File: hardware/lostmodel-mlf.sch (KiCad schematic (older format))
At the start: 17 parts, among them IC1 ATMEGA88P, K1 CONN_3, P1 ISP, Q1 BC847C

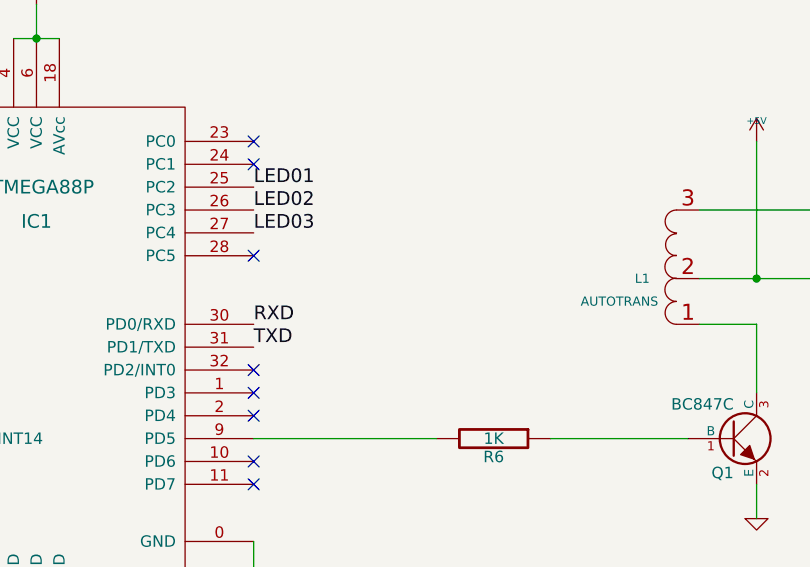
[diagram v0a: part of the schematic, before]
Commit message: Added UART break-out to PCB for possible future debug (or other) use.
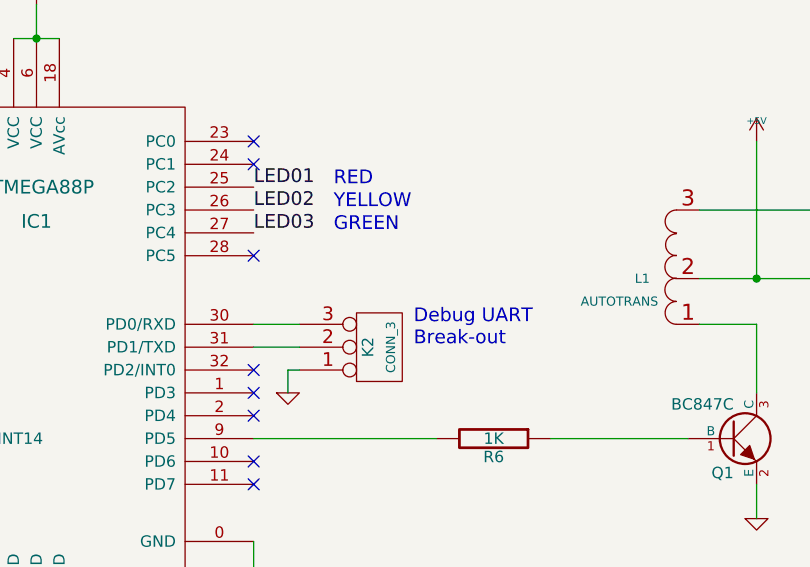
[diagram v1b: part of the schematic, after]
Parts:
- added K2: CONN_3, symbol CONN_3
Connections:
- net GND: now also K2.1 (P1)
- net RXD: no longer names the net of IC1.30 (PD0/RXD)
- net RXD: now also K2.3 (P3)
- net TXD: no longer names the net of IC1.31 (PD1/TXD)
- net TXD: now also K2.2 (PM)
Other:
- note added: "Debug UART\nBreak-out"
- note added: "GREEN"
- note added: "RED"
- note added: "YELLOW"
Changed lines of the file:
@@
 Sheet 1 1
 Title "Lost Model Alarm"
-Date "24 nov 2014"
-Rev "1.0"
+Date "28 nov 2014"
+Rev "1.1"
 Comp ""
 Comment1 ""
@@
 $EndComp
 $Comp
-L +5V #PWR01
+L +5V #PWR12
 U 1 1 51A74974
 P 8700 3800
-F 0 "#PWR01" H 8700 3890 20  0001 C CNN
+F 0 "#PWR12" H 8700 3890 20  0001 C CNN
 F 1 "+5V" H 8700 3890 30  0000 C CNN
 F 2 "" H 8700 3800 60  0001 C CNN
@@
 $EndComp
 $Comp
-L GND #PWR02
+L GND #PWR13
 U 1 1 51A74963
 P 8700 5450
-F 0 "#PWR02" H 8700 5450 30  0001 C CNN
+F 0 "#PWR13" H 8700 5450 30  0001 C CNN
 F 1 "GND" H 8700 5380 30  0001 C CNN
 F 2 "" H 8700 5450 60  0001 C CNN
@@
 $EndComp
 $Comp
-L GND #PWR03
+L GND #PWR8
 U 1 1 51A744A2
 P 6150 2350
-F 0 "#PWR03" H 6150 2350 30  0001 C CNN
+F 0 "#PWR8" H 6150 2350 30  0001 C CNN
 F 1 "GND" H 6150 2280 30  0001 C CNN
 F 2 "" H 6150 2350 60  0001 C CNN
@@
 	1    0    0    -1
 $EndComp
-Text Label 6500 4700 0    60   ~ 0
-TXD
 NoConn ~ 4550 4000
 NoConn ~ 4550 3900
@@
 Text Label 6500 4000 0    60   ~ 0
 LED01
-Text Label 6500 4600 0    60   ~ 0
-RXD
-$Comp
-L +5V #PWR04
+$Comp
+L +5V #PWR1
 U 1 1 504AC376
 P 3100 2650
-F 0 "#PWR04" H 3100 2740 20  0001 C CNN
+F 0 "#PWR1" H 3100 2740 20  0001 C CNN
 F 1 "+5V" H 3100 2740 30  0000 C CNN
 F 2 "" H 3100 2650 60  0001 C CNN
@@
 $EndComp
 $Comp
-L +5V #PWR05
+L +5V #PWR10
 U 1 1 4ED08824
 P 7750 1350
-F 0 "#PWR05" H 7750 1440 20  0001 C CNN
+F 0 "#PWR10" H 7750 1440 20  0001 C CNN
 F 1 "+5V" H 7750 1440 30  0000 C CNN
 F 2 "" H 7750 1350 60  0001 C CNN
@@
 $EndComp
 $Comp
-L GND #PWR06
+L GND #PWR11
 U 1 1 4ED08810
 P 7750 2250
-F 0 "#PWR06" H 7750 2250 30  0001 C CNN
+F 0 "#PWR11" H 7750 2250 30  0001 C CNN
 F 1 "GND" H 7750 2180 30  0001 C CNN
 F 2 "" H 7750 2250 60  0001 C CNN
@@
 $EndComp
 $Comp
-L +5V #PWR07
+L +5V #PWR3
 U 1 1 4ECC4A1D
 P 3100 4400
-F 0 "#PWR07" H 3100 4490 20  0001 C CNN
+F 0 "#PWR3" H 3100 4490 20  0001 C CNN
 F 1 "+5V" H 3100 4490 30  0000 C CNN
 F 2 "" H 3100 4400 60  0001 C CNN
@@
 MOSI
 $Comp
-L GND #PWR08
+L GND #PWR7
 U 1 1 4ECC4963
 P 5550 6250
-F 0 "#PWR08" H 5550 6250 30  0001 C CNN
+F 0 "#PWR7" H 5550 6250 30  0001 C CNN
 F 1 "GND" H 5550 6180 30  0001 C CNN
 F 2 "" H 5550 6250 60  0001 C CNN
@@
 $EndComp
 $Comp
-L +5V #PWR09
+L +5V #PWR6
 U 1 1 4ECC494B
 P 5550 3200
-F 0 "#PWR09" H 5550 3290 20  0001 C CNN
+F 0 "#PWR6" H 5550 3290 20  0001 C CNN
 F 1 "+5V" H 5550 3290 30  0000 C CNN
 F 2 "" H 5550 3200 60  0001 C CNN
@@
 MISO
 $Comp
-L GND #PWR010
+L GND #PWR2
 U 1 1 4ECB2F15
 P 3100 3550
-F 0 "#PWR010" H 3100 3550 30  0001 C CNN
+F 0 "#PWR2" H 3100 3550 30  0001 C CNN
 F 1 "GND" H 3100 3480 30  0001 C CNN
 F 2 "" H 3100 3550 60  0001 C CNN
@@
 $EndComp
 $Comp
-L GND #PWR012
+L GND #PWR5
 U 1 1 5470FFF7
 P 3250 2150
-F 0 "#PWR012" H 3250 2150 30  0001 C CNN
+F 0 "#PWR5" H 3250 2150 30  0001 C CNN
 F 1 "GND" H 3250 2080 30  0001 C CNN
 F 2 "" H 3250 2150 60  0001 C CNN
@@
 	2900 1950 3250 1950
 $Comp
-L +5V #PWR013
+L +5V #PWR4
 U 1 1 54710003
 P 3250 1350
-F 0 "#PWR013" H 3250 1440 20  0001 C CNN
+F 0 "#PWR4" H 3250 1440 20  0001 C CNN
 F 1 "+5V" H 3250 1440 30  0000 C CNN
 F 2 "" H 3250 1350 60  0001 C CNN
@@
 Wire Wire Line
 	3100 4500 3100 4400
+Text Notes 6850 4000 0    60   ~ 0
+RED
+Text Notes 6850 4100 0    60   ~ 0
+YELLOW
+Text Notes 6850 4200 0    60   ~ 0
+GREEN
+Text Notes 7200 4700 0    60   ~ 0
+Debug UART\nBreak-out
+$Comp
+L CONN_3 K2
+U 1 1 5478F3CC
+P 7050 4700
+F 0 "K2" V 7000 4700 50  0000 C CNN
+F 1 "CONN_3" V 7100 4700 40  0000 C CNN
+F 2 "" H 7050 4700 60  0000 C CNN
+F 3 "" H 7050 4700 60  0000 C CNN
+	1    7050 4700
+	1    0    0    1
+$EndComp
+Wire Wire Line
+	6700 4600 6500 4600
+Wire Wire Line
+	6700 4700 6500 4700
+Wire Wire Line
+	6700 4800 6650 4800
+$Comp
+L GND #PWR9
+U 1 1 5478F49D
+P 6650 4900
+F 0 "#PWR9" H 6650 4900 30  0001 C CNN
+F 1 "GND" H 6650 4830 30  0001 C CNN
+F 2 "" H 6650 4900 60  0001 C CNN
+F 3 "" H 6650 4900 60  0001 C CNN
+	1    6650 4900
+	1    0    0    -1
+$EndComp
+Wire Wire Line
+	6650 4800 6650 4900
 $EndSCHEMATC

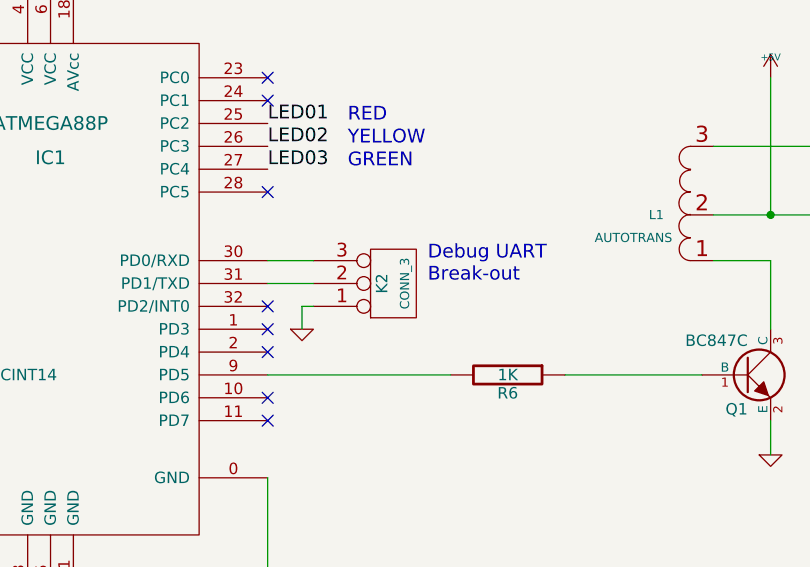
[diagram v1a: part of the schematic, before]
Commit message: PCB v1.1 tidying after Gerber view check.
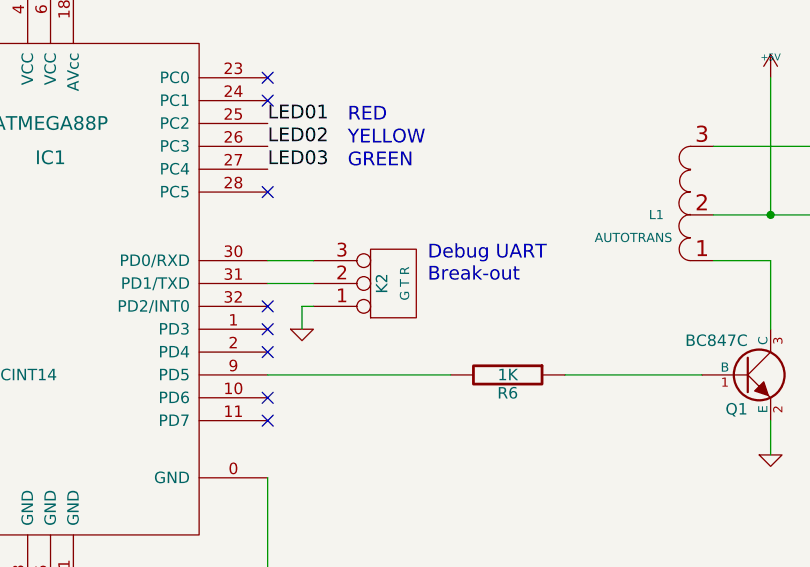
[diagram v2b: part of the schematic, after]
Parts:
- K2: value CONN_3 -> G T R
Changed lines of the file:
@@
 $EndComp
 $Comp
-L +5V #PWR12
+L +5V #PWR01
 U 1 1 51A74974
 P 8700 3800
-F 0 "#PWR12" H 8700 3890 20  0001 C CNN
+F 0 "#PWR01" H 8700 3890 20  0001 C CNN
 F 1 "+5V" H 8700 3890 30  0000 C CNN
 F 2 "" H 8700 3800 60  0001 C CNN
@@
 $EndComp
 $Comp
-L GND #PWR13
+L GND #PWR02
 U 1 1 51A74963
 P 8700 5450
-F 0 "#PWR13" H 8700 5450 30  0001 C CNN
+F 0 "#PWR02" H 8700 5450 30  0001 C CNN
 F 1 "GND" H 8700 5380 30  0001 C CNN
 F 2 "" H 8700 5450 60  0001 C CNN
@@
 $EndComp
 $Comp
-L GND #PWR8
+L GND #PWR03
 U 1 1 51A744A2
 P 6150 2350
-F 0 "#PWR8" H 6150 2350 30  0001 C CNN
+F 0 "#PWR03" H 6150 2350 30  0001 C CNN
 F 1 "GND" H 6150 2280 30  0001 C CNN
 F 2 "" H 6150 2350 60  0001 C CNN
@@
 LED01
 $Comp
-L +5V #PWR1
+L +5V #PWR04
 U 1 1 504AC376
 P 3100 2650
-F 0 "#PWR1" H 3100 2740 20  0001 C CNN
+F 0 "#PWR04" H 3100 2740 20  0001 C CNN
 F 1 "+5V" H 3100 2740 30  0000 C CNN
 F 2 "" H 3100 2650 60  0001 C CNN
@@
 $EndComp
 $Comp
-L +5V #PWR10
+L +5V #PWR05
 U 1 1 4ED08824
 P 7750 1350
-F 0 "#PWR10" H 7750 1440 20  0001 C CNN
+F 0 "#PWR05" H 7750 1440 20  0001 C CNN
 F 1 "+5V" H 7750 1440 30  0000 C CNN
 F 2 "" H 7750 1350 60  0001 C CNN
@@
 $EndComp
 $Comp
-L GND #PWR11
+L GND #PWR06
 U 1 1 4ED08810
 P 7750 2250
-F 0 "#PWR11" H 7750 2250 30  0001 C CNN
+F 0 "#PWR06" H 7750 2250 30  0001 C CNN
 F 1 "GND" H 7750 2180 30  0001 C CNN
 F 2 "" H 7750 2250 60  0001 C CNN
@@
 $EndComp
 $Comp
-L +5V #PWR3
+L +5V #PWR07
 U 1 1 4ECC4A1D
 P 3100 4400
-F 0 "#PWR3" H 3100 4490 20  0001 C CNN
+F 0 "#PWR07" H 3100 4490 20  0001 C CNN
 F 1 "+5V" H 3100 4490 30  0000 C CNN
 F 2 "" H 3100 4400 60  0001 C CNN
@@
 MOSI
 $Comp
-L GND #PWR7
+L GND #PWR08
 U 1 1 4ECC4963
 P 5550 6250
-F 0 "#PWR7" H 5550 6250 30  0001 C CNN
+F 0 "#PWR08" H 5550 6250 30  0001 C CNN
 F 1 "GND" H 5550 6180 30  0001 C CNN
 F 2 "" H 5550 6250 60  0001 C CNN
@@
 $EndComp
 $Comp
-L +5V #PWR6
+L +5V #PWR09
 U 1 1 4ECC494B
 P 5550 3200
-F 0 "#PWR6" H 5550 3290 20  0001 C CNN
+F 0 "#PWR09" H 5550 3290 20  0001 C CNN
 F 1 "+5V" H 5550 3290 30  0000 C CNN
 F 2 "" H 5550 3200 60  0001 C CNN
@@
 MISO
 $Comp
-L GND #PWR2
+L GND #PWR010
 U 1 1 4ECB2F15
 P 3100 3550
-F 0 "#PWR2" H 3100 3550 30  0001 C CNN
+F 0 "#PWR010" H 3100 3550 30  0001 C CNN
 F 1 "GND" H 3100 3480 30  0001 C CNN
 F 2 "" H 3100 3550 60  0001 C CNN
@@
 $EndComp
 $Comp
-L GND #PWR5
+L GND #PWR011
 U 1 1 5470FFF7
 P 3250 2150
-F 0 "#PWR5" H 3250 2150 30  0001 C CNN
+F 0 "#PWR011" H 3250 2150 30  0001 C CNN
 F 1 "GND" H 3250 2080 30  0001 C CNN
 F 2 "" H 3250 2150 60  0001 C CNN
@@
 	2900 1950 3250 1950
 $Comp
-L +5V #PWR4
+L +5V #PWR012
 U 1 1 54710003
 P 3250 1350
-F 0 "#PWR4" H 3250 1440 20  0001 C CNN
+F 0 "#PWR012" H 3250 1440 20  0001 C CNN
 F 1 "+5V" H 3250 1440 30  0000 C CNN
 F 2 "" H 3250 1350 60  0001 C CNN
@@
 P 7050 4700
 F 0 "K2" V 7000 4700 50  0000 C CNN
-F 1 "CONN_3" V 7100 4700 40  0000 C CNN
+F 1 "G  T  R" V 7100 4700 40  0000 C CNN
 F 2 "" H 7050 4700 60  0000 C CNN
 F 3 "" H 7050 4700 60  0000 C CNN
@@
 	6700 4800 6650 4800
 $Comp
-L GND #PWR9
+L GND #PWR013
 U 1 1 5478F49D
 P 6650 4900
-F 0 "#PWR9" H 6650 4900 30  0001 C CNN
+F 0 "#PWR013" H 6650 4900 30  0001 C CNN
 F 1 "GND" H 6650 4830 30  0001 C CNN
 F 2 "" H 6650 4900 60  0001 C CNN

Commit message: Completing KiCAD upgrade changes
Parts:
- C1: footprint (none) -> gruvin:SM0603_GRUVIN; symbol C -> C-RESCUE-lostmodel-mlf
- C2: footprint (none) -> gruvin:SM1210_GRUVIN_POL
- D1, D3: footprint (none) -> gruvin:LED-0603
- D2: value YELLOW -> BLUE; footprint (none) -> gruvin:LED-0603
- IC1: footprint (none) -> gruvin:MLF-32_2mmVIA_SINK
- K1, K2: footprint (none) -> gruvin:SIL-3
- L1: footprint ~ -> gruvin:TRI-3
- P1: footprint (none) -> gruvin:PIN_ARRAY_3x2_GRUVIN
- PZ1: footprint (none) -> gruvin:PIN_ARRAY_2X1
- Q1: footprint (none) -> gruvin:SOT23-BCE
- R1, R2, R3, R4, R5, R6: footprint (none) -> gruvin:SM0603; symbol R -> R-RESCUE-lostmodel-mlf
